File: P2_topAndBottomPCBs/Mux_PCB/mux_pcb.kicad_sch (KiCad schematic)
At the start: 104 parts, among them J1 Conn_02x12_Odd_Even, J10 Conn_02x06_Odd_Even, J11 Conn_01x02, J12 Conn_01x02, J13 Conn_02x06_Odd_Even, J14 Conn_01x02, J15 Conn_02x06_Odd_Even, J16 Conn_01x02, J17 Conn_02x06_Odd_Even, J18 Conn_02x06_Odd_Even, J19 Conn_01x02, J2 Banana, J20 Conn_01x02, J21 Conn_02x06_Odd_Even, J22 Conn_01x02, J24 Conn_01x02, J25 Conn_01x8, J27 Conn_01x02, J3 Banana, J30 Conn_01x02, J32 Conn_01x02, J34 Conn_01x02, J35 Conn_01x8, J36 Conn_01x02, J39 Conn_01x02, J4 Conn_01x8, J40 Conn_01x06, J5 Conn_01x10, J6 Conn_01x02, J7 Conn_02x06_Odd_Even, J8 Conn_02x06_Odd_Even, J9 Conn_01x02, U1 AZ1084CD-3.3TRG1, U2 AMS1117-1.8, U3 CD74HC4053PWR

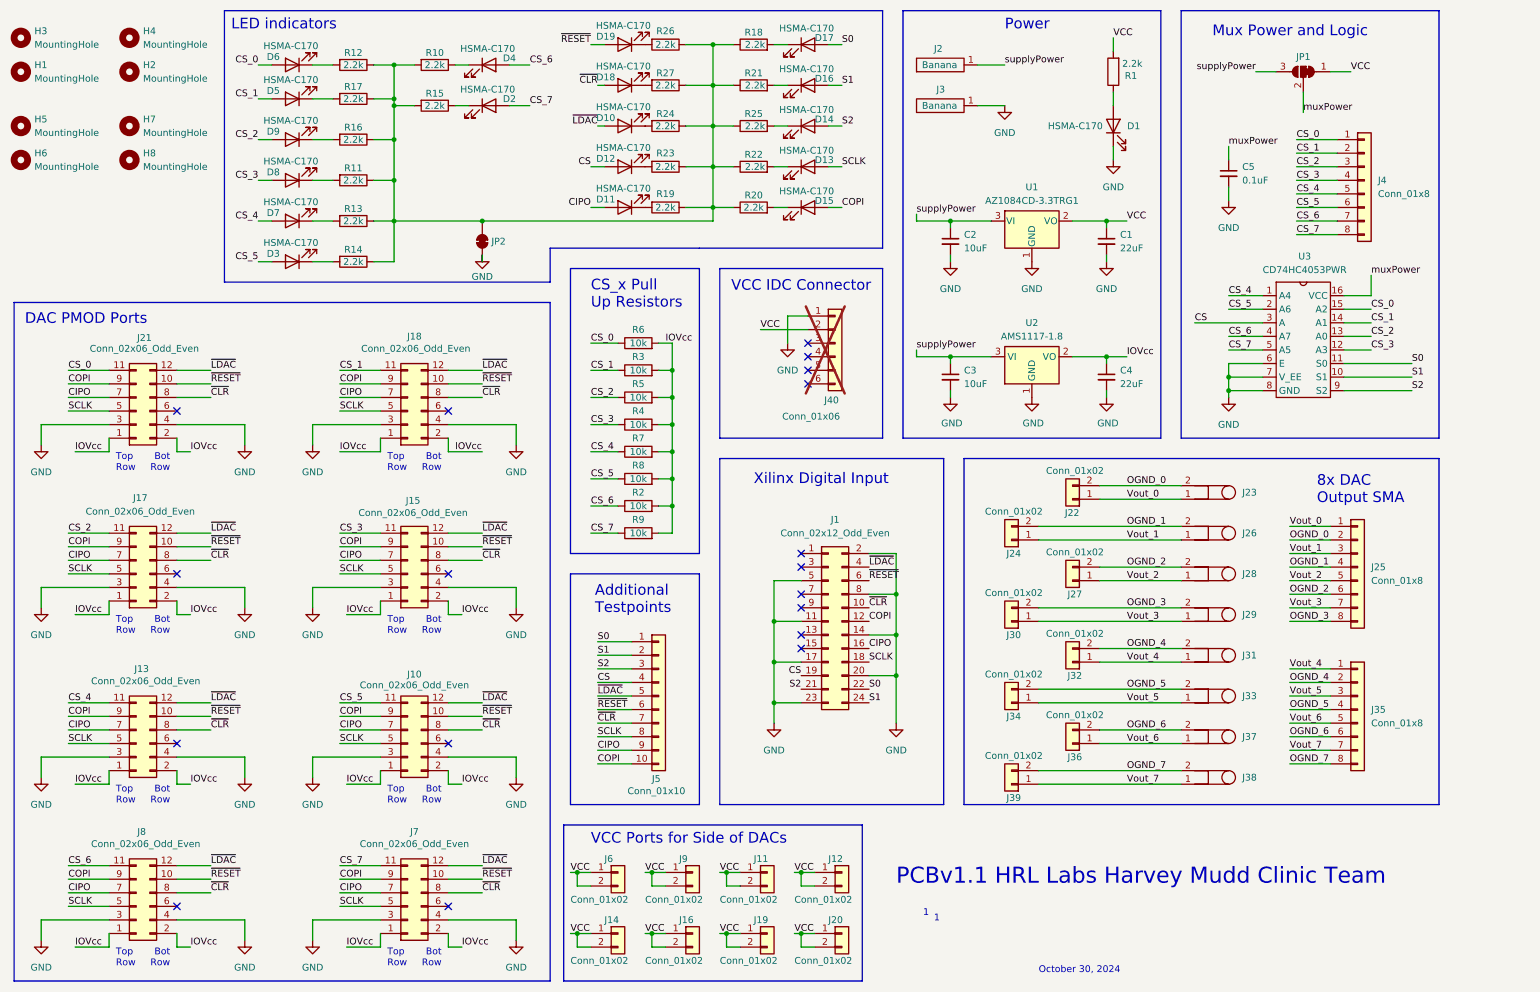
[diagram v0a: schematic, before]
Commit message: Separated PCB into two PCBS
Ordering as one PCB w/ V-cut was more expensive. Also fixed placement for JLCPCB orders and narrowed the mux board since it no longer needs to be 70mm wide
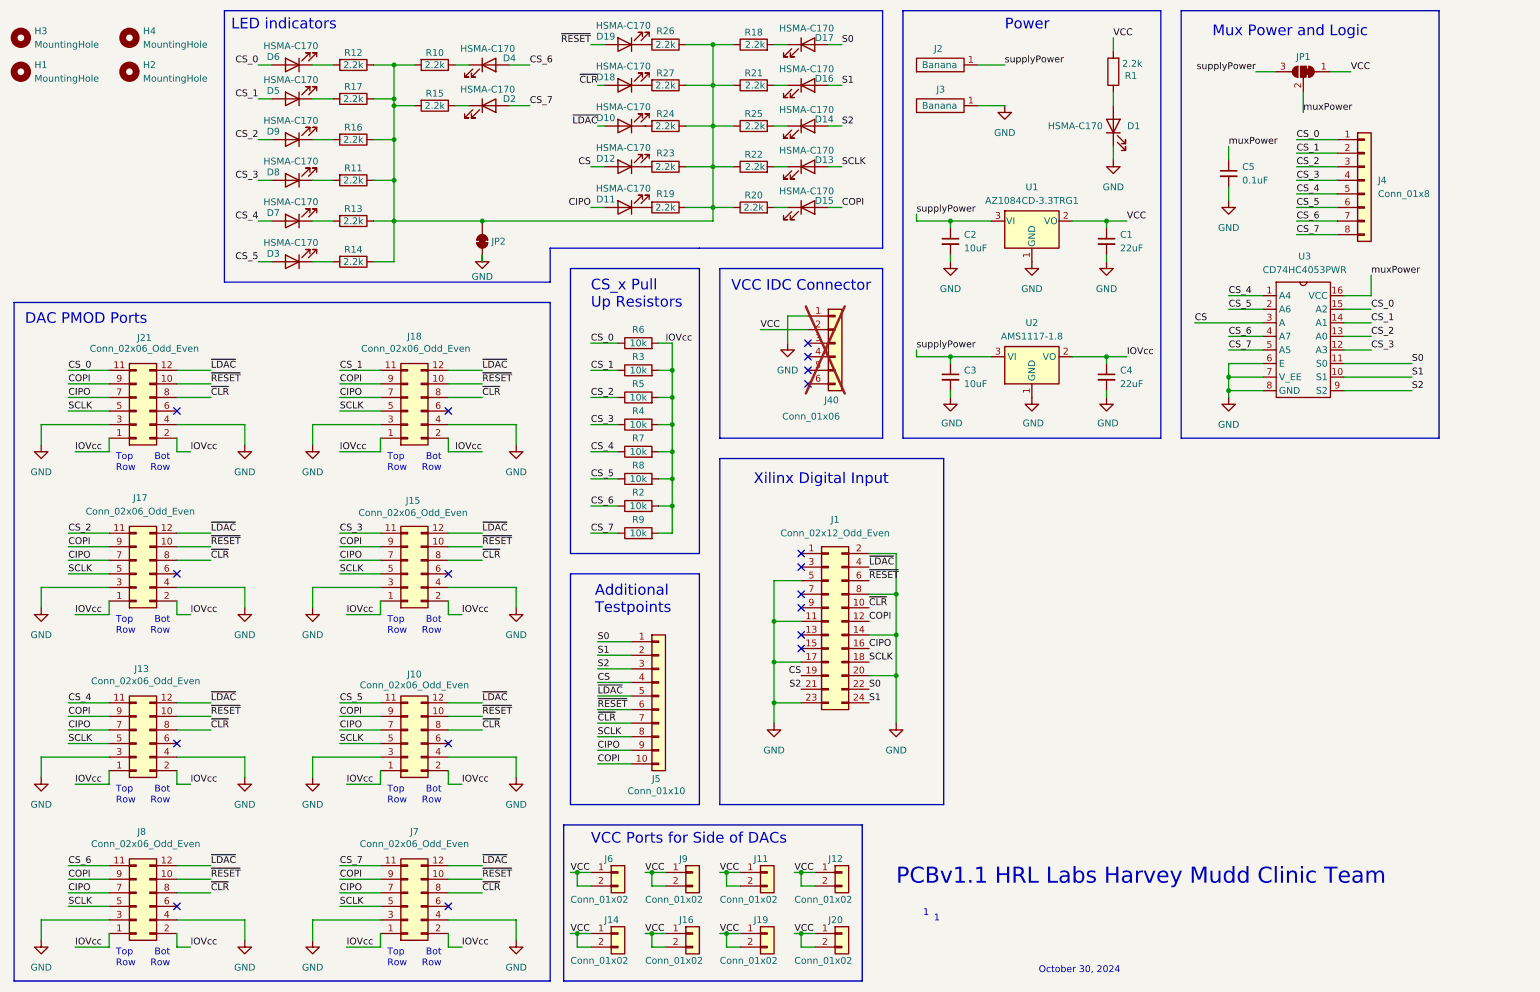
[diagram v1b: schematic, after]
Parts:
- removed H5, H6, H7, H8: MountingHole, MountingHole:MountingHole_3.2mm_M3, symbol Mechanical:MountingHole
- removed J22, J24, J27, J30, J32, J34, J36, J39: Conn_01x02, Connector_PinSocket_2.54mm:PinSocket_1x02_P2.54mm_Vertical, symbol Connector_Generic:Conn_01x02
- removed J23, J26, J28, J29, J31, J33, J37, J38: ~, Connector_Coaxial:SMA_Amphenol_132134-16_Vertical, symbol HRL_Custom:SMA_Connector
- removed J25, J35: Conn_01x8, Connector_PinHeader_2.54mm:PinHeader_1x08_P2.54mm_Vertical, symbol Connector_Generic:Conn_01x08
- J1: JLCPCB Position Offset (none) -> 0.5,0; JLCPCB Rotation Offset (none) -> -90
- J10, J13, J15, J17, J18, J21, J7, J8: JLCPCB Position Offset (none) -> 4.2,0; JLCPCB Rotation Offset (none) -> -90
- J11, J12, J14, J16, J19, J20, J4, J5, J6, J9: JLCPCB Rotation Offset (none) -> -90
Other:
- note removed: "8x DAC Output SMA"
